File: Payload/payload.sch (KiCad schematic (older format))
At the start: 24 parts

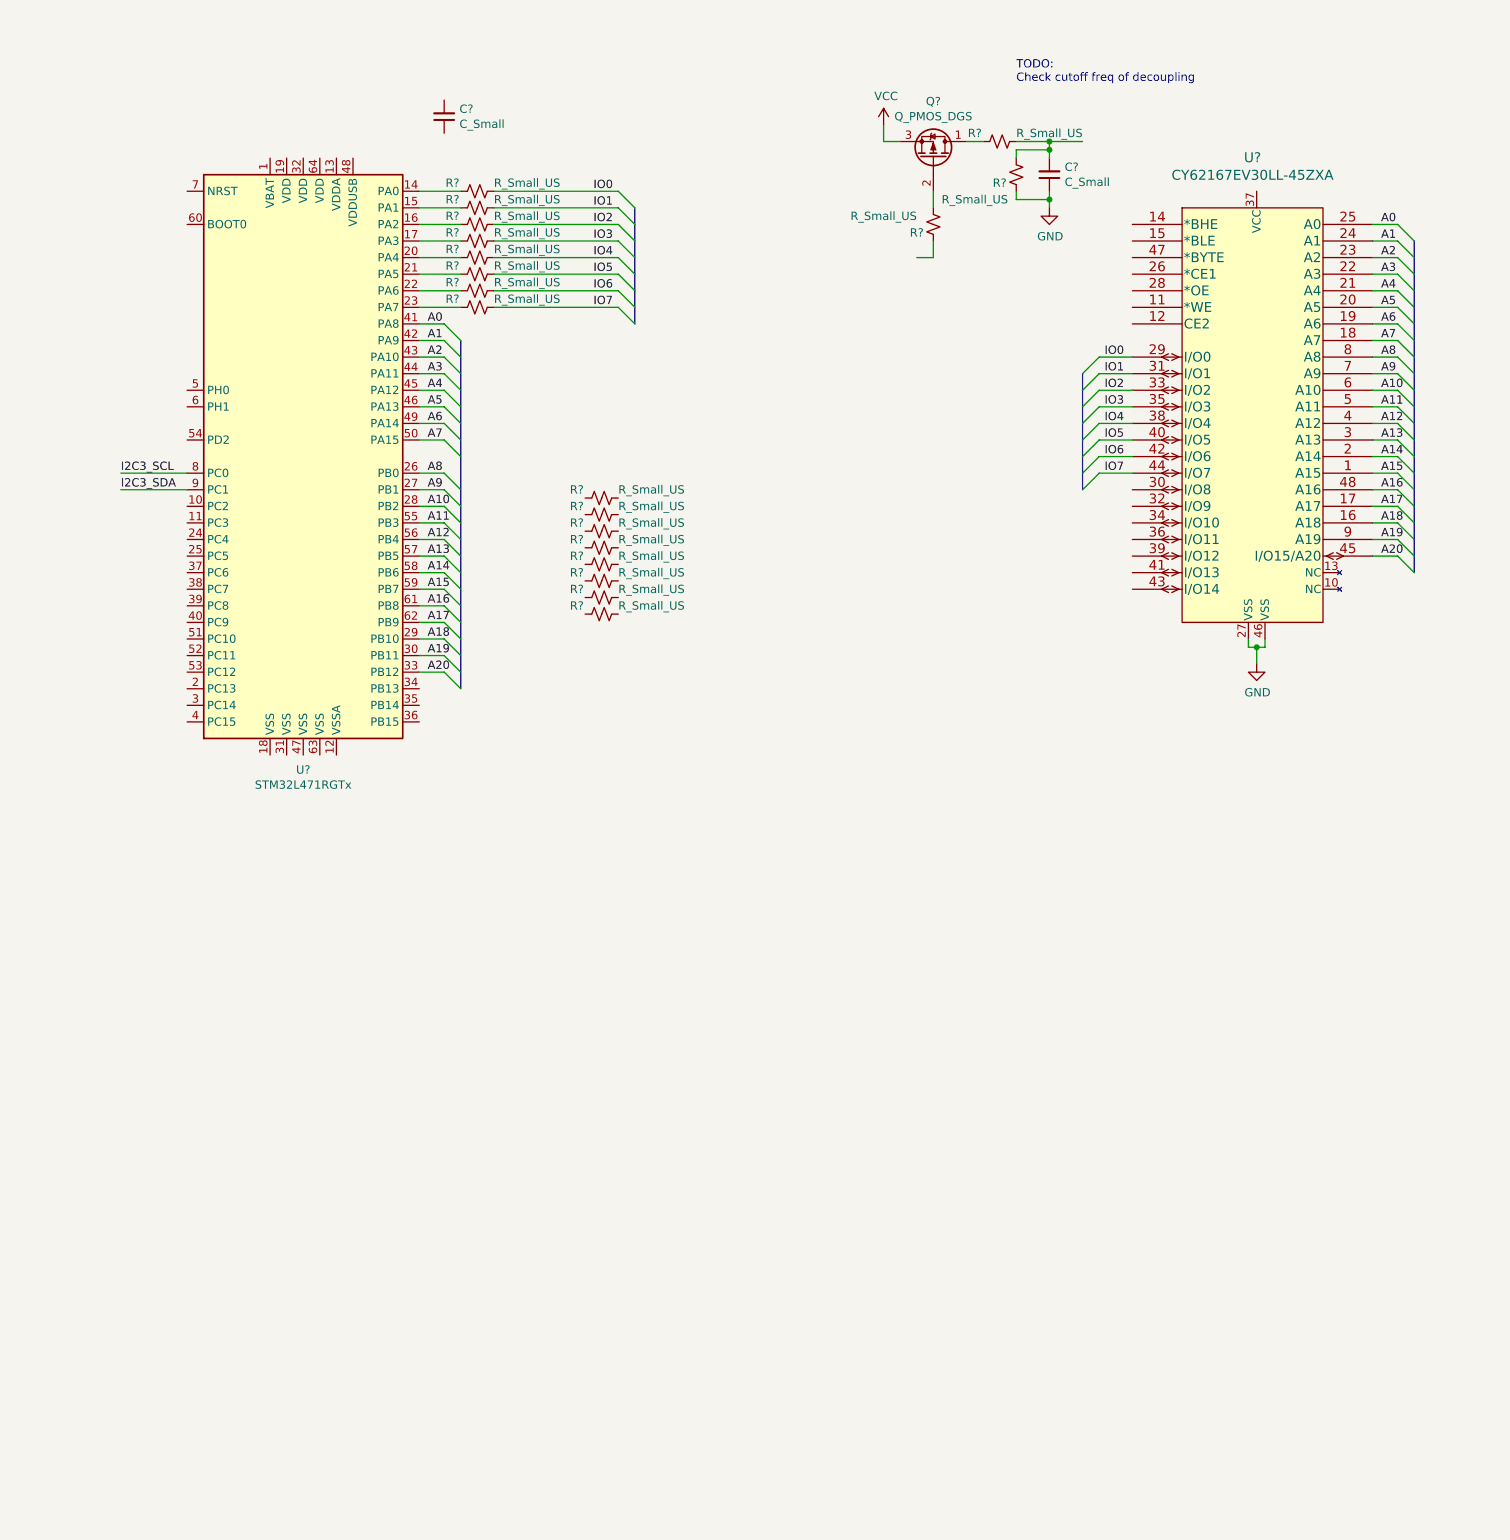
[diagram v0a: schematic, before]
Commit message: Work on bus and power
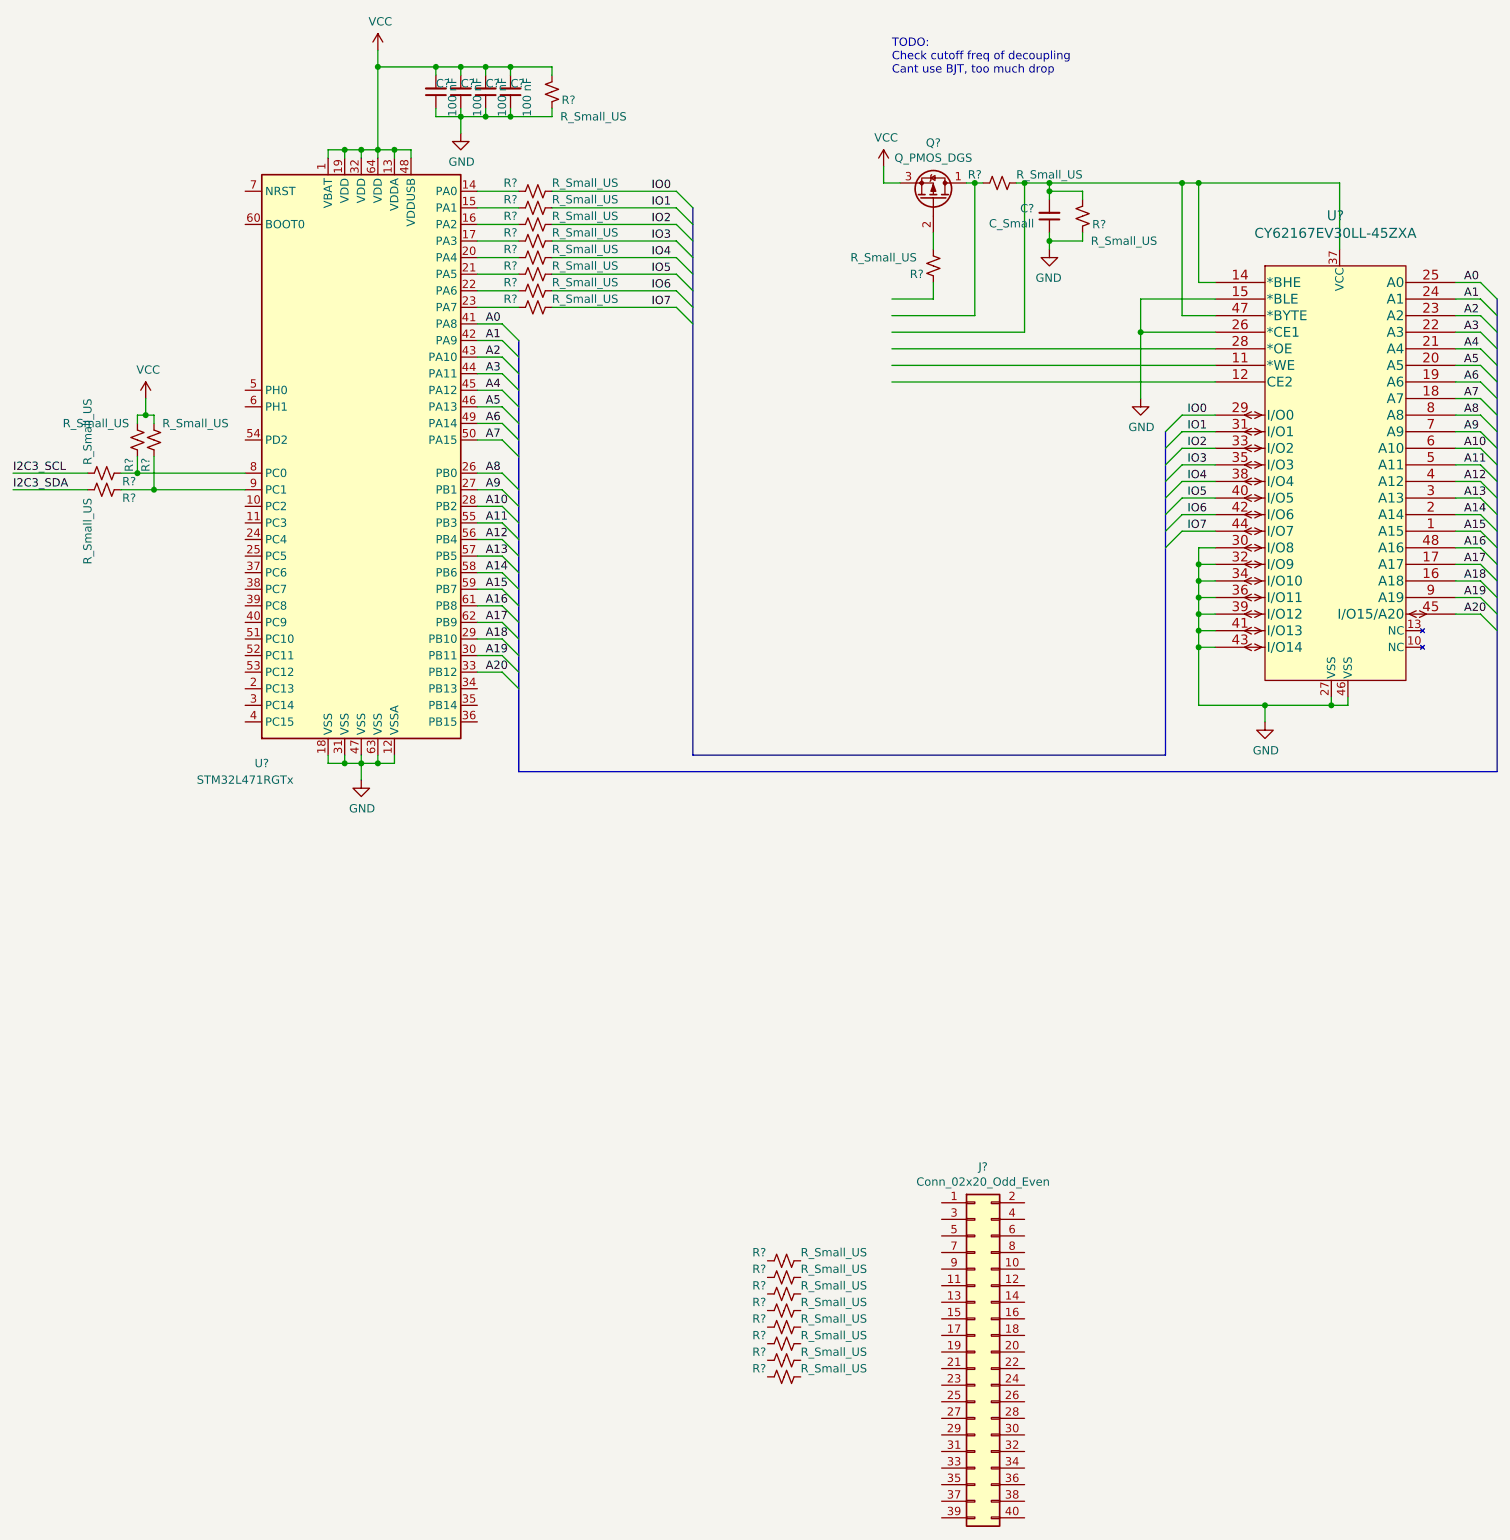
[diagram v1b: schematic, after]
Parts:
- added C? (x3): 100 nF, symbol Device:C_Small
- added J?: Conn_02x20_Odd_Even, symbol Connector_Generic:Conn_02x20_Odd_Even
- added R? (x5): R_Small_US, symbol Device:R_Small_US
- C?: value C_Small -> 100 nF
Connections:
- wire segments 89 -> 178
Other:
- note added: "TODO:\nCheck cutoff freq of decoupling\nCant use BJT, too much drop"
- note removed: "TODO:\nCheck cutoff freq of decoupling"
- moved on the sheet: C?, Q?, R?, U?

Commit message: Progress on bus
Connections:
- net labels added: M1_CE
- wire segments 178 -> 188
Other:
- moved on the sheet: J?, R?
